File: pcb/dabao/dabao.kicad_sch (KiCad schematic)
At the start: 67 parts, among them J1 Conn_01x05, J2 USB_C_Receptacle_USB2.0_16P, J3 Conn_01x04, J4 MagConn_01x04_Pin, J5 Conn_Battery, J7 Conn_01x04, J8 Display, SW1 SW_RESET, SW2 SW_POWER, U1 nice_nano, U2 MCP23017_SP

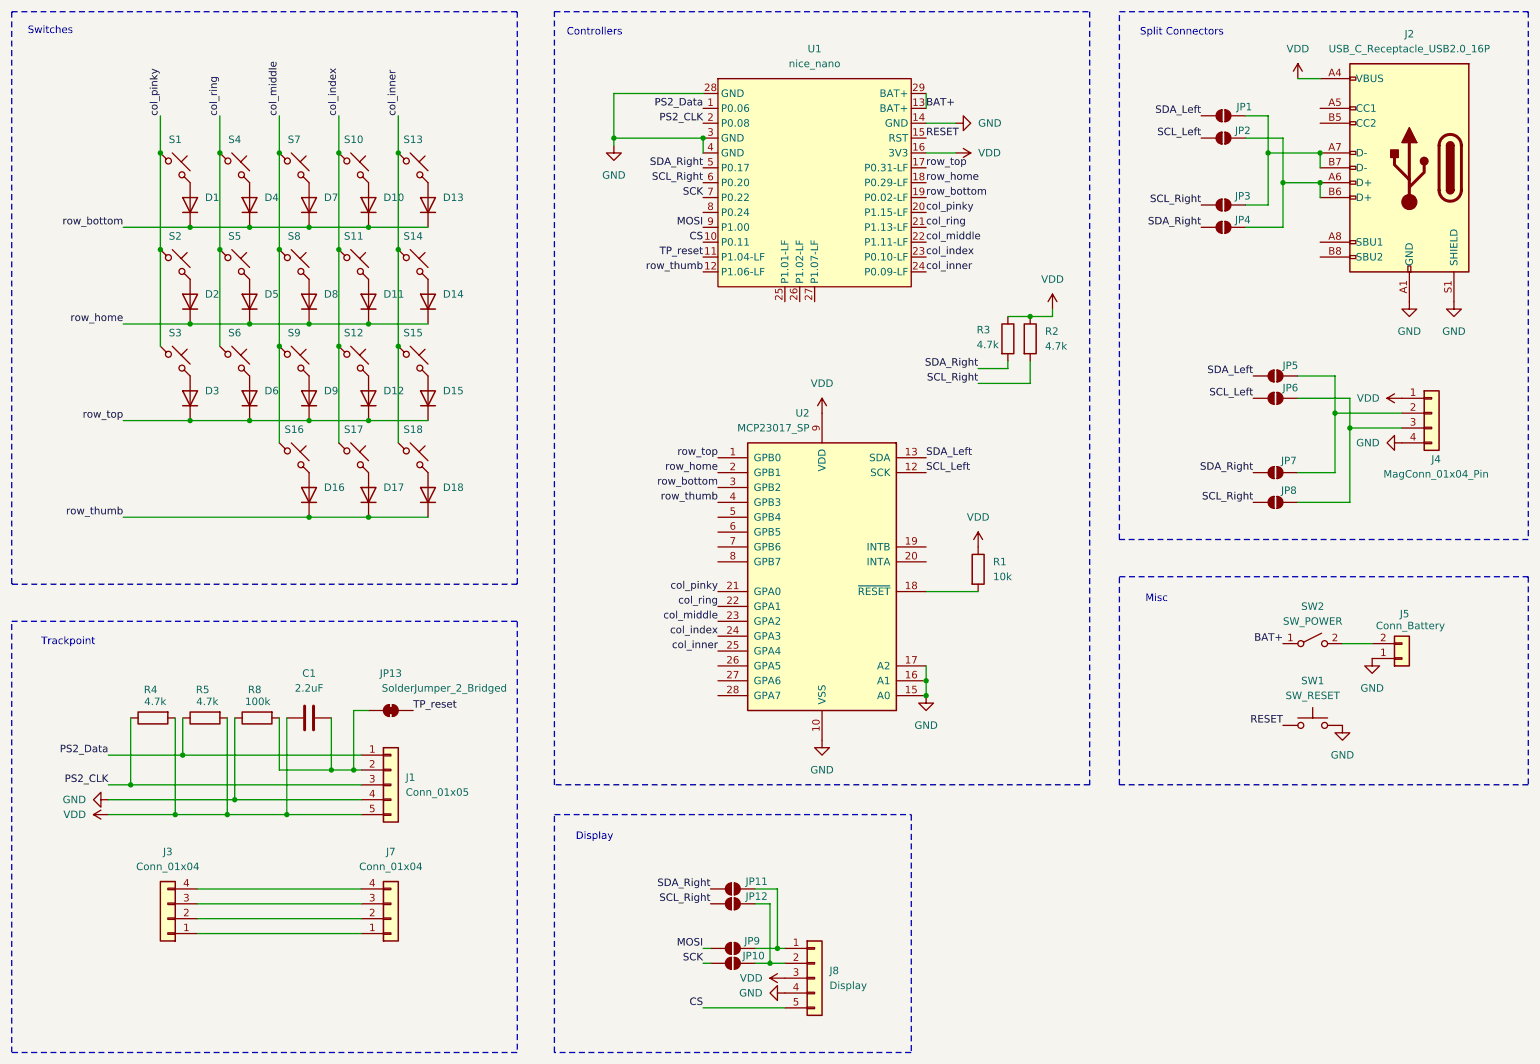
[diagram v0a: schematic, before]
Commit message: Touchpoint power MOSFET, decoupling cap for GPIO expander
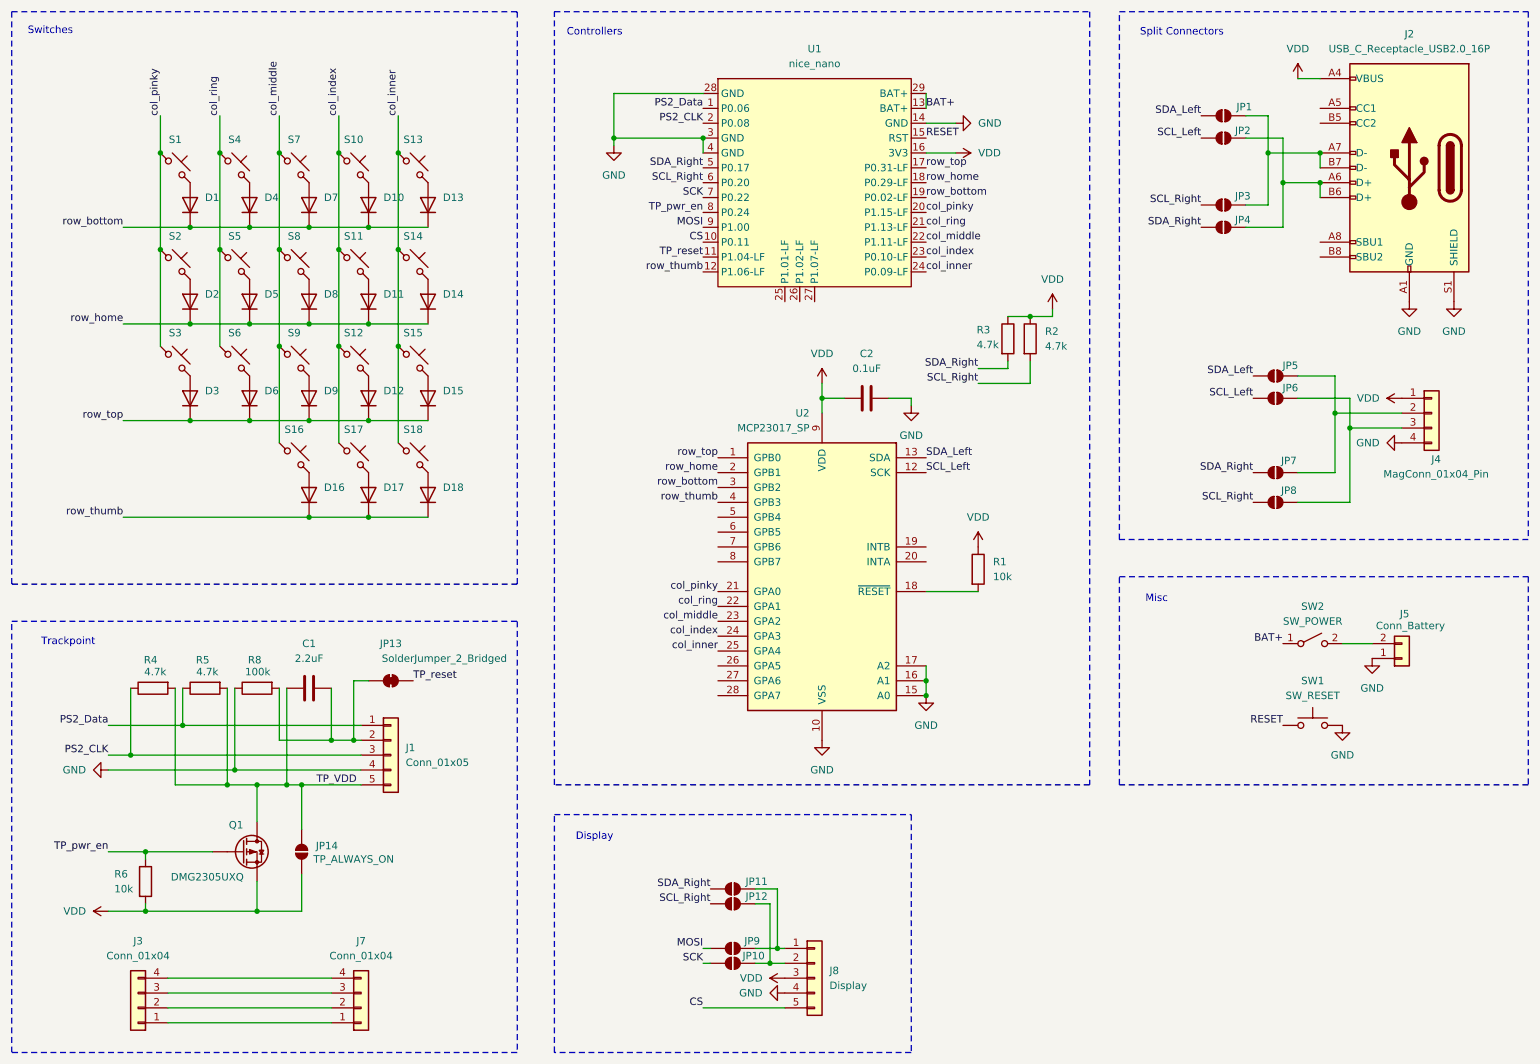
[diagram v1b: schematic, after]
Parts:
- added C2: 0.1uF, Capacitor_SMD:C_0805_2012Metric, symbol Device:C
- added JP14: TP_ALWAYS_ON, Jumper:SolderJumper-2_P1.3mm_Open_TrianglePad1.0x1.5mm, symbol Jumper:SolderJumper_2_Open
- added Q1: DMG2305UXQ, Library:DMG2305UXQ, symbol Device:Q_PMOS
- added R6: 10k, Resistor_SMD:R_0805_2012Metric, symbol Device:R
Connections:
- net GND: now also C2.2
- net VDD: now also C2.1, JP14.1 (A), Q1.S, R6.2; no longer C1.1, J1.5 (Pin_5), R4.2, R5.2
- net TP_pwr_en: now reaches U1.8 (P0.24)
- net TP_pwr_en: now also Q1.G, R6.1
- new net TP_VDD: C1.1, J1.5 (Pin_5), JP14.2 (B), Q1.D, R4.2, R5.2
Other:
- moved on the sheet: C1, J1, J3, J7, JP13, R4, R5, R8

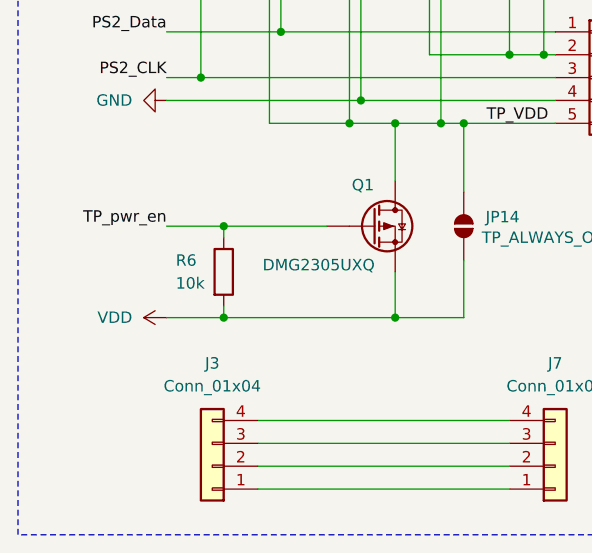
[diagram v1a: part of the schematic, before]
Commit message: Increase the value of R6 to reduce power draw when touchpoint is enabled
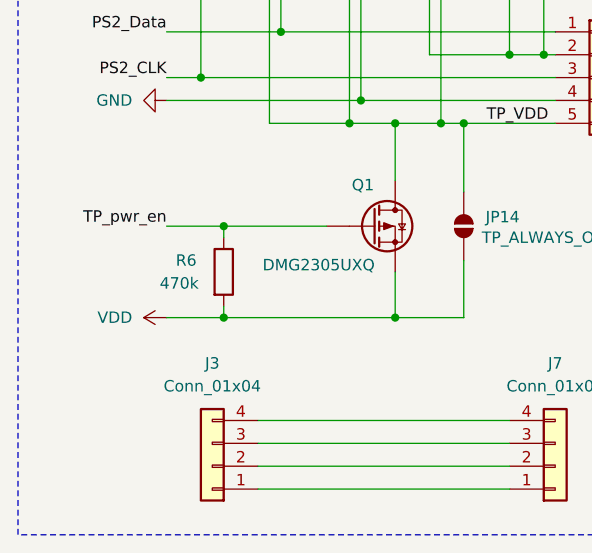
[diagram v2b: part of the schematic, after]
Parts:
- R6: value 10k -> 470k
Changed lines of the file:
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@@
 			)
 		)
-		(property "Value" "10k"
-			(at 36.576 165.1 0)
+		(property "Value" "470k"
+			(at 34.798 165.1 0)
 			(show_name no)
 			(do_not_autoplace no)
